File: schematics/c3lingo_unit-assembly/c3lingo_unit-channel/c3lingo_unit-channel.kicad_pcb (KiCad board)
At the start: 2 copper layers, 75 x 183 mm, 124 parts, among them J301 Mic X In, J302 Headphone X, J303 PowerSupply, J304 Inputs, J305 Output, J306 PowerSupply, J307 Interconnect, J308 Interconnect, SW301 OnAir_X, SW302 Mute_X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

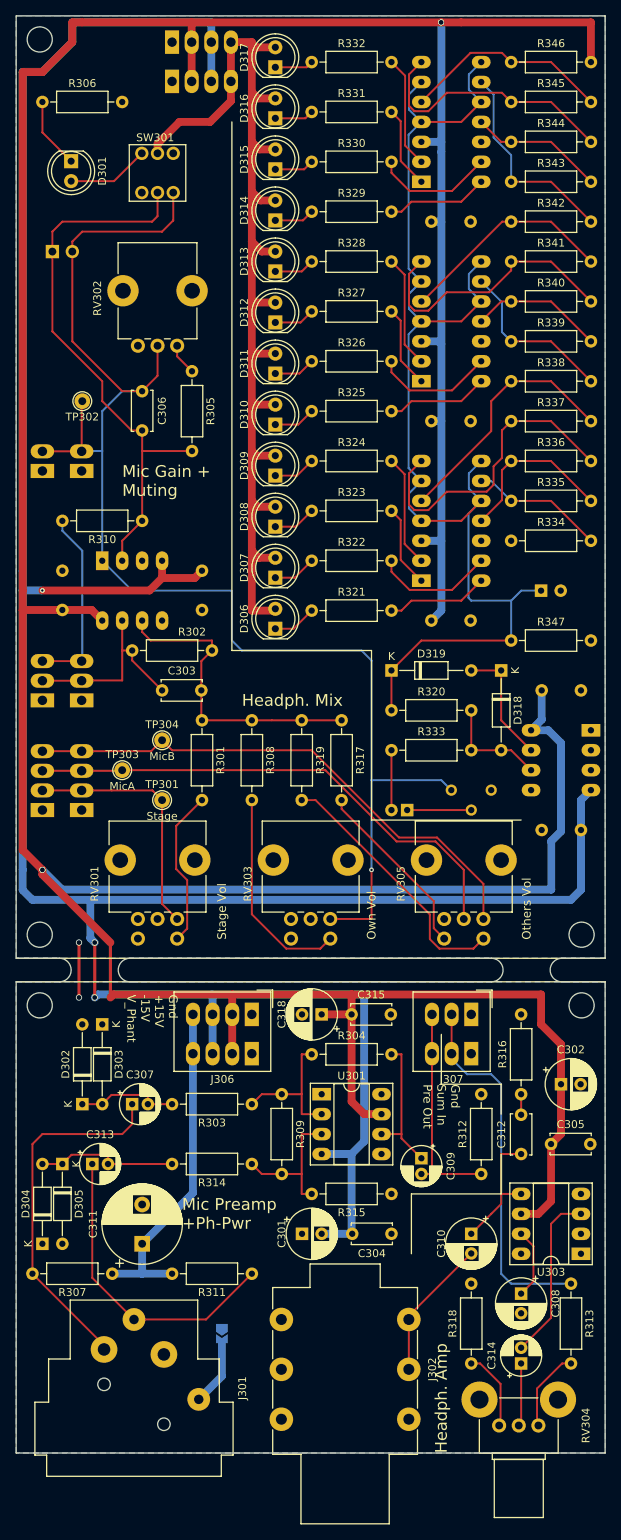
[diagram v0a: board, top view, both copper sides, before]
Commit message: PCB: Update for new schematic (still THT for now)
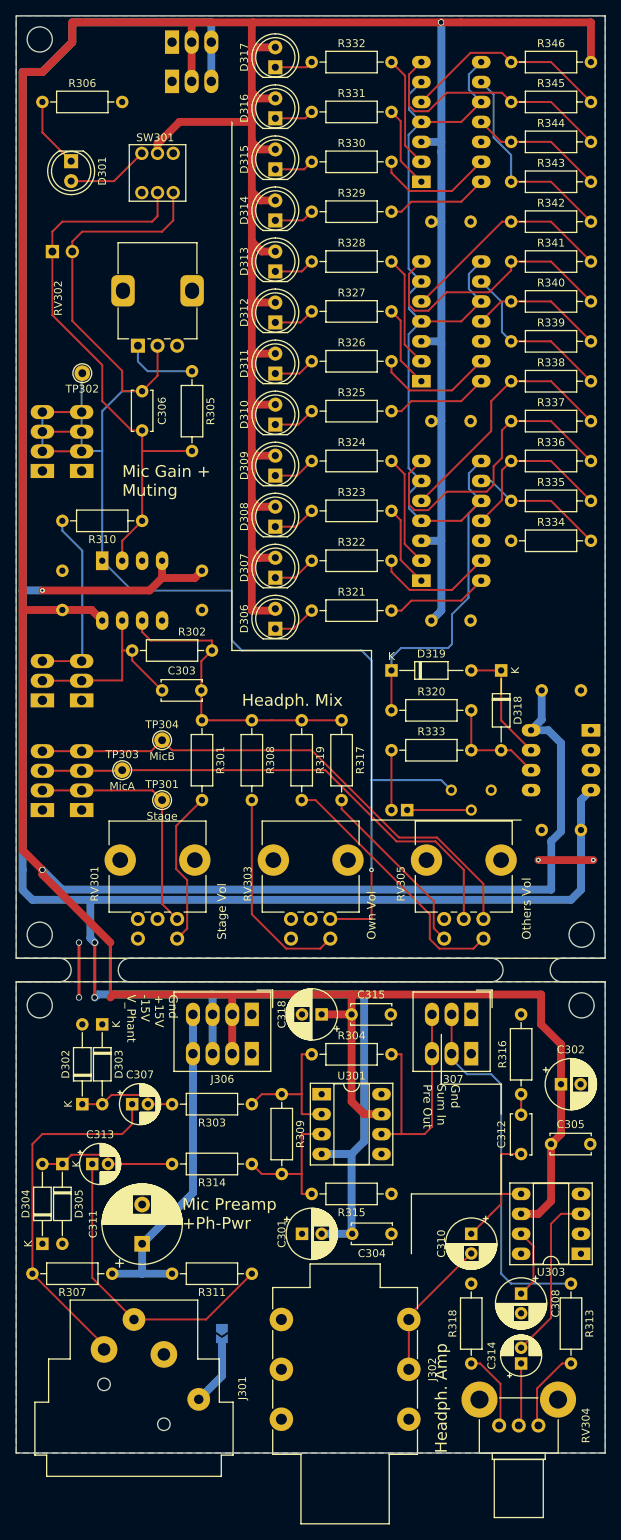
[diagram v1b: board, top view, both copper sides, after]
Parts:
- removed C309: 1uF, Capacitor_THT:CP_Radial_D5.0mm_P2.00mm
- removed C320: 47uF, Capacitor_THT:CP_Radial_D6.3mm_P2.50mm
- removed R312: 820R, Resistor_THT:R_Axial_DIN0207_L6.3mm_D2.5mm_P10.16mm_Horizontal
- removed R347: 100K, Resistor_THT:R_Axial_DIN0207_L6.3mm_D2.5mm_P10.16mm_Horizontal
- J303: footprint TerminalBlock_Phoenix:TerminalBlock_Phoenix_PTSM-0,5-4-2.5-H-THR_1x04_P2.50mm_Horizontal -> TerminalBlock_Phoenix:TerminalBlock_Phoenix_PTSM-0,5-3-2.5-H-THR_1x03_P2.50mm_Horizontal
- J305: footprint TerminalBlock_Phoenix:TerminalBlock_Phoenix_PTSM-0,5-2-2.5-H-THR_1x02_P2.50mm_Horizontal -> TerminalBlock_Phoenix:TerminalBlock_Phoenix_PTSM-0,5-4-2.5-H-THR_1x04_P2.50mm_Horizontal
- R306: value 390R -> 680R
- moved RV302 5.00 mm to (65.5, 92.0)
- moved TP302 3.56 mm to (58.4, 95.5)
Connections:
- D306 pad 2: V_LED -> +15V
- D307 pad 2: V_LED -> +15V
- D308 pad 2: V_LED -> +15V
- D309 pad 2: V_LED -> +15V
- D310 pad 2: V_LED -> +15V
- D311 pad 2: V_LED -> +15V
- D312 pad 2: V_LED -> +15V
- D313 pad 2: V_LED -> +15V
- D314 pad 2: V_LED -> +15V
- D315 pad 2: V_LED -> +15V
- D316 pad 2: V_LED -> +15V
- D317 pad 2: V_LED -> +15V
- R304 pad 2: Net-(C309-Pad1) -> MicPreOut
- SW301 pad 5: V_LED -> +15V
- U301 pad 6: Net-(C309-Pad1) -> MicPreOut
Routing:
- net V_LED: track 134.6 -> 0.00 mm
- net +15V: track 521.2 -> 649.8 mm
- net /PreampOut: track 179.6 -> 198.2 mm
- net Net-(C309-Pad1): track 18.1 -> 0.00 mm
- net Net-(D319-Pad1): track 157.6 -> 142.6 mm
- net GND: track 0.00 -> 14.0 mm, vias 0 -> 4
- net (no net): track 7.00 -> 0.00 mm, vias 2 -> 0
- net Net-(R305-Pad1): track 4.03 -> 9.41 mm
- net MicPreOut: track 29.2 -> 32.7 mm
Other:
- board text added: "Gnd Mic X (3x)"
- board text added: "c3lingo Interpreter Unit v0.3 2022-12-30 Jannik Beyerstedt (jtbx)"
- board text added: "c3lingo Interpreter Unit v0.3 2023-12-30 Jannik Beyerstedt (jtbx)"
- board text removed: "Gnd Mic X"
- board text removed: "c3lingo Interpreter Unit v0.2 2021-05-30 Jannik Beyerstedt (jtbx)"

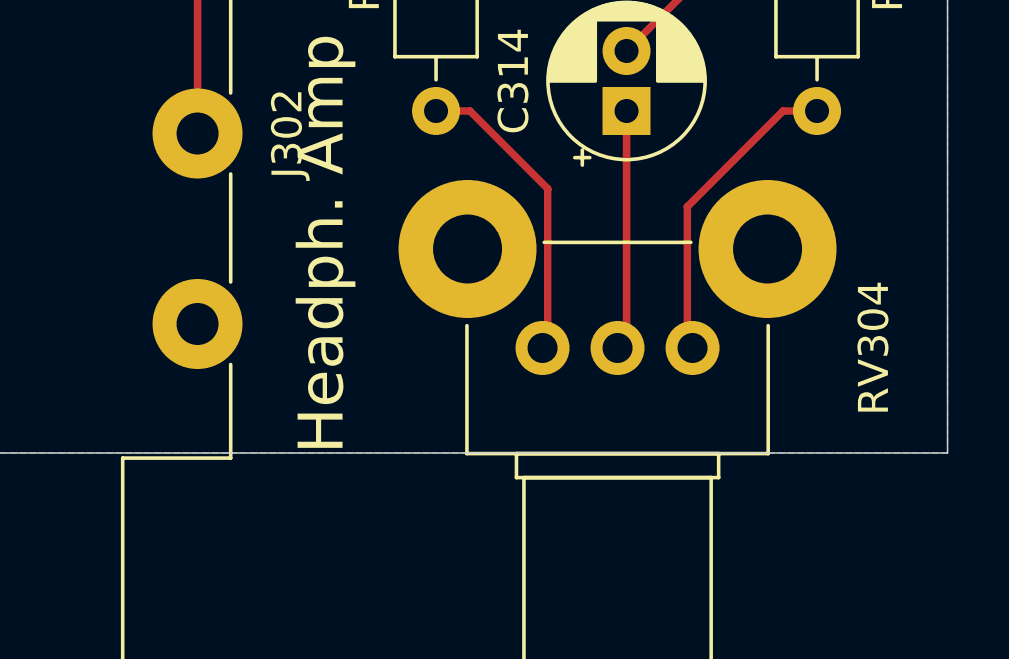
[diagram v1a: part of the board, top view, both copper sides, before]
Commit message: Update footprints to KiCad 6
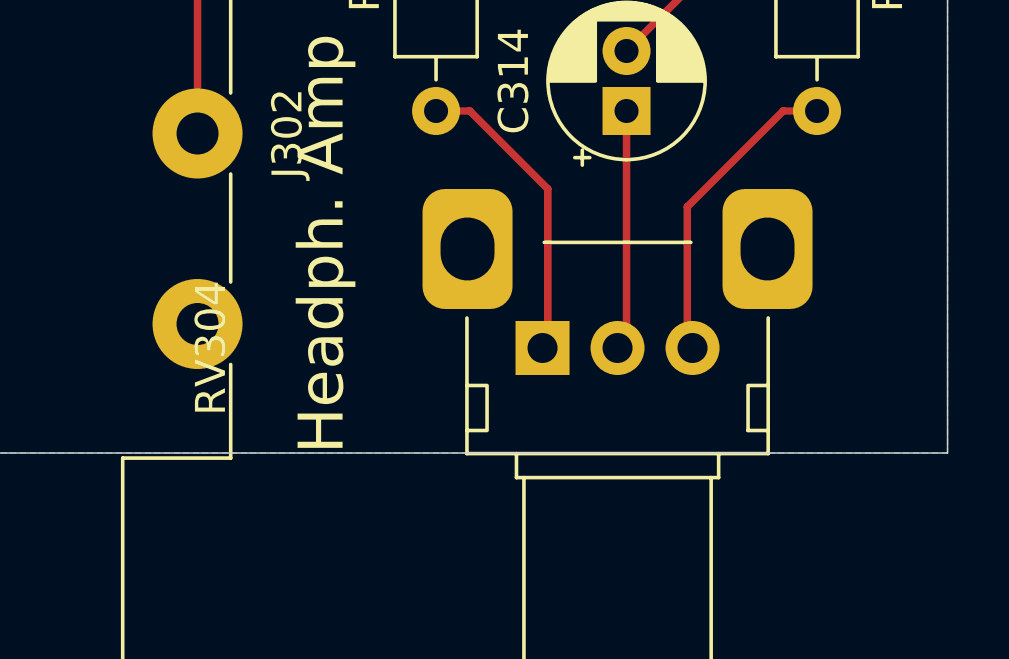
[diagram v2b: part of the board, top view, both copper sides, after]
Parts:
- turned RV304 to 90 degrees
